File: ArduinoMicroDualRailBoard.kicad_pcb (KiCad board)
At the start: 2 copper layers, 135.3 x 92.7 mm, 56 parts, among them J1 Conn_01x20_Male, J10 Conn_01x02_Male, J2 Screw_Terminal_01x03, J3 Conn_01x20_Male, J4 Conn_01x20_Male, J5 Screw_Terminal_01x03, J6 Conn_01x20_Male, J7 SDS-50J, J8 SDS-50J, J9 Screw_Terminal_01x03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

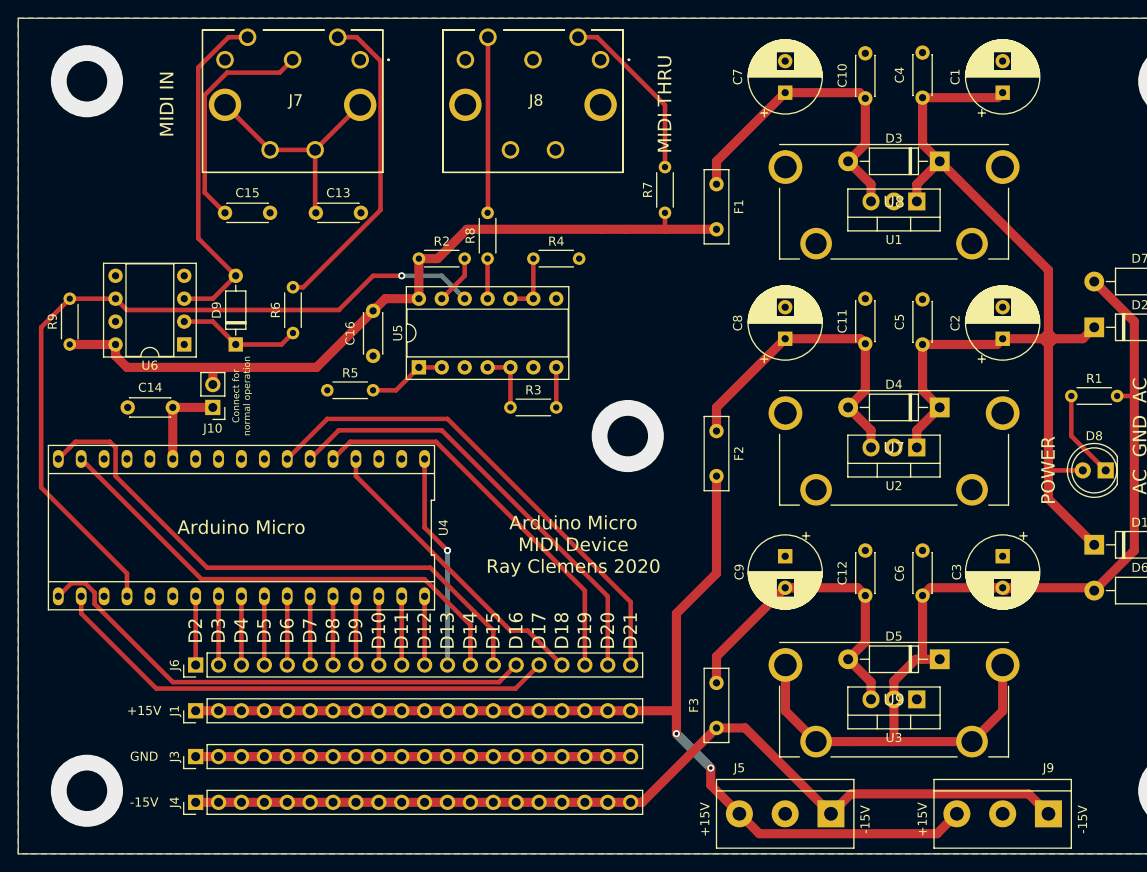
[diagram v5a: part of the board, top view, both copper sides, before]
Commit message: Lots of small fixes * Added protection diodes on +/- 15V rails * Fixed 7915 diode direction * Flipped Arduino socket so the USB can actually be plugged in * Added +5V out (since it might be useful to have)
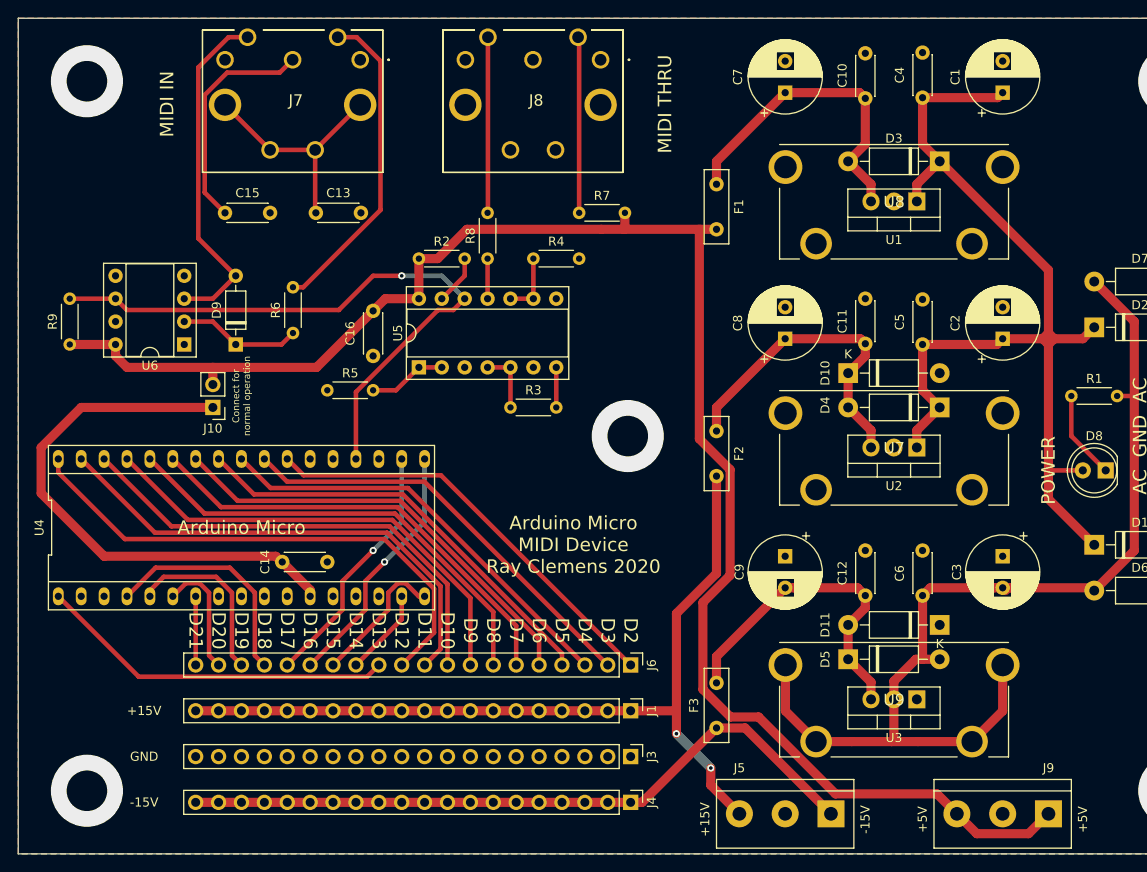
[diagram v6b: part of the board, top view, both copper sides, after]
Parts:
- added D10: 1N4001, Diode_THT:D_DO-41_SOD81_P10.16mm_Horizontal, F.Cu at (176.5, 91.4)
- added D11: 1N4001, Diode_THT:D_DO-41_SOD81_P10.16mm_Horizontal, F.Cu at (186.7, 119.4)
- moved J1 48.3 mm to (152.4, 128.9), turned to 270 degrees
- moved J3 48.3 mm to (152.4, 134.0), turned to 270 degrees
- moved J4 48.3 mm to (152.4, 139.1), turned to 270 degrees
- moved J6 48.3 mm to (152.4, 123.8), turned to 270 degrees
- moved C14 28.0 mm to (118.7, 112.4), turned to 180 degrees
- moved R7 10.8 mm to (146.7, 73.7), turned to 0 degrees
- moved D5 10.2 mm to (176.5, 123.2), turned to 0 degrees
- turned U4 to 0 degrees
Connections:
- D5 pad 1: -VDC -> Net-(C12-Pad2)
- D5 pad 2: Net-(C12-Pad2) -> -VDC
- J9 pad 1: -15V -> +5V
- J9 pad 3: +15V -> +5V
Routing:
- net +5V: track 86.4 -> 186.0 mm
- net Net-(C14-Pad2): track 9.53 -> 61.0 mm
- net /D12: track 7.62 -> 58.5 mm
- net GND: track 52.7 -> 4.44 mm, vias 0 -> 5
- net /D15: track 63.7 -> 15.6 mm
- net /D21: track 55.3 -> 7.62 mm
- net /D11: track 7.62 -> 55.2 mm
- net /D14: track 55.2 -> 9.72 mm
- net /D10: track 7.62 -> 52.8 mm
- net /D9: track 7.62 -> 51.9 mm
- net /D8: track 7.62 -> 51.0 mm
- net /D7: track 7.62 -> 50.1 mm
- net /D6: track 7.62 -> 49.2 mm
- net /D5: track 7.62 -> 48.3 mm
- net /D3: track 7.62 -> 47.6 mm
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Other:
- board text added: "+5V"
